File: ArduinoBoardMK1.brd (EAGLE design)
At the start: 95.2 x 82.5 mm, 24 parts

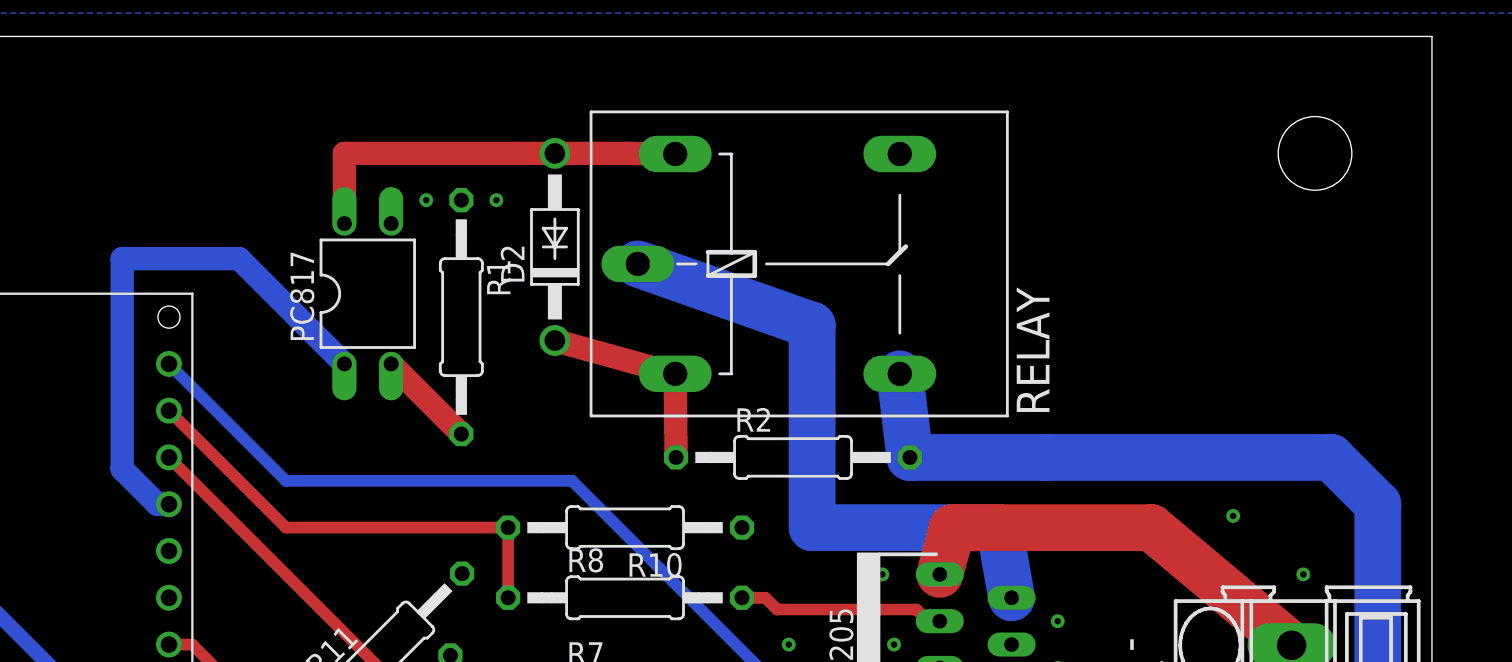
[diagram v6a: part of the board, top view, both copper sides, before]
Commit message: Solid State Relay
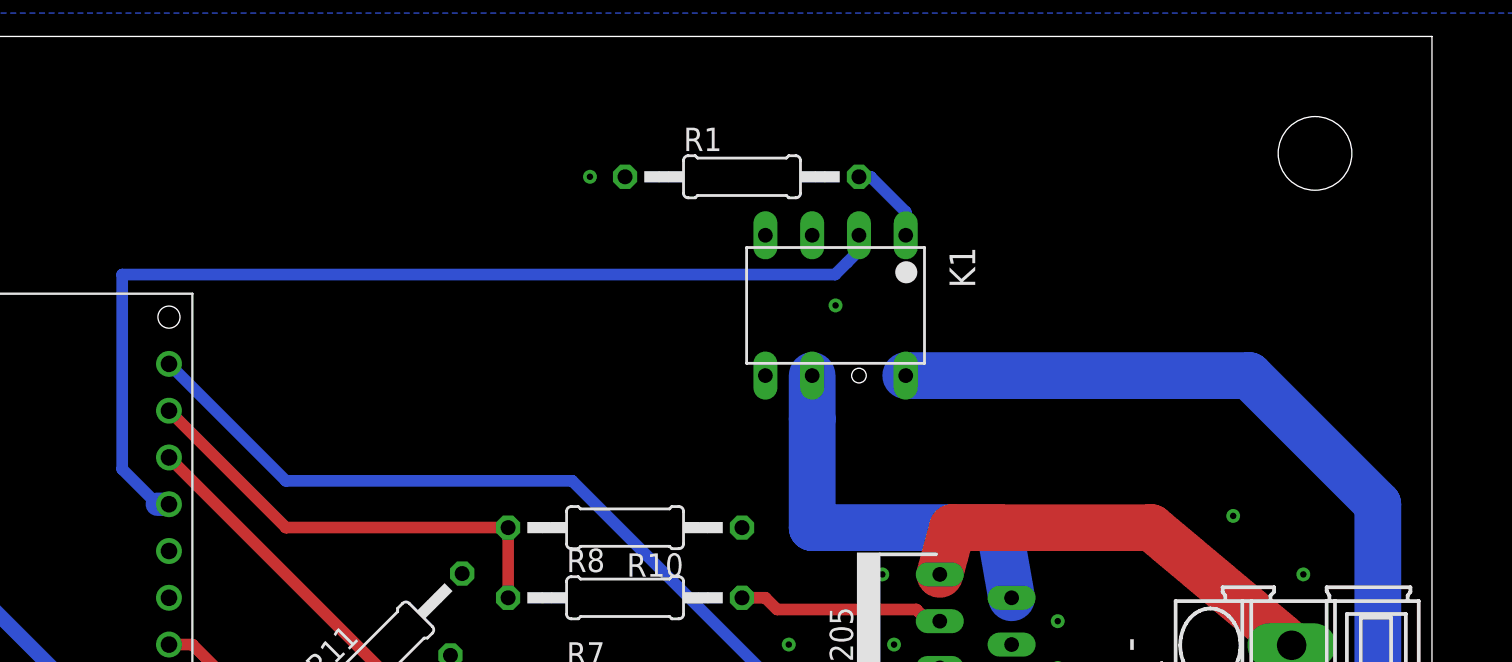
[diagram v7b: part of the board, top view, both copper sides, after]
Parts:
- removed D2: 1N4004, diode:DO41-10
- removed PC817: PC817, optocoupler:DIL04
- removed R2: 220, resistor:0207/12
- removed RELAY: G5LE, relay:G5LE
- added K1: AQH2223, relay:DIL07
- moved R1 17.0 mm to (57.8, 74.9), turned to 0 degrees
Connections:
- removed net FLYBACK-DIODE+: D2.C, R2.1, RELAY.1
- removed net RELAY-TO-OPTO: D2.A, PC817.4, RELAY.2
- net +12V: now also K1.8; no longer R2.2, RELAY.S
- net GND: no longer PC817.3
- net MOTOR-ENABLE: now also K1.2; no longer PC817.1
- net POST-OPTO-DIODE: now also K1.1; no longer PC817.2
- net RELAY-TO-MOTORCONTROLLER: now also K1.6; no longer RELAY.P
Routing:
- net MOTOR-ENABLE: track 29.2 -> 55.3 mm
- net RELAY-TO-OPTO: track 21.8 -> 0.00 mm
- net RELAY-TO-MOTORCONTROLLER: track 35.0 -> 22.3 mm
- net FLYBACK-DIODE+: track 11.3 -> 0.00 mm
- net +12V: track 101.6 -> 99.1 mm
- net POST-OPTO-DIODE: track 5.39 -> 4.60 mm
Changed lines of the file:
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@@
 <drawing>
 <settings>
-<setting alwaysvectorfont="no"/>
+<setting alwaysvectorfont="yes"/>
 <setting verticaltext="up"/>
 </settings>
-<grid distance="0.025" unitdist="inch" unit="mil" style="lines" multiple="1" display="no" altdistance="5" altunitdist="mil" altunit="mil"/>
+<grid distance="0.025" unitdist="inch" unit="inch" style="lines" multiple="1" display="no" altdistance="5" altunitdist="mil" altunit="mil"/>
 <layers>
 <layer number="1" name="Top" color="4" fill="1" visible="yes" active="yes"/>
@@
 <hole x="88.9" y="6.35" drill="4"/>
 <hole x="6.35" y="6.35" drill="4"/>
+<hole x="64.135" y="64.135" drill="0.79501875"/>
 </plain>
 <attributes>
@@
 <element name="R7" library="resistor" library_urn="urn:adsk.eagle:library:348" package="0207/12" package3d_urn="urn:adsk.eagle:package:25938/1" value="1k" x="51.435" y="46.99"/>
 <element name="R8" library="resistor" library_urn="urn:adsk.eagle:library:348" package="0207/12" package3d_urn="urn:adsk.eagle:package:25938/1" value="1k" x="51.435" y="52.07"/>
-<element name="RELAY" library="relay" library_urn="urn:adsk.eagle:library:339" package="G5LE" package3d_urn="urn:adsk.eagle:package:24308/1" value="G5LE" x="61.653509375" y="70.19810625">
-<attribute name="MF" value="" x="61.653509375" y="70.19810625" size="1.778" layer="27" display="off"/>
-<attribute name="MPN" value="" x="61.653509375" y="70.19810625" size="1.778" layer="27" display="off"/>
-<attribute name="OC_FARNELL" value="unknown" x="61.653509375" y="70.19810625" size="1.778" layer="27" display="off"/>
-<attribute name="OC_NEWARK" value="unknown" x="61.653509375" y="70.19810625" size="1.778" layer="27" display="off"/>
-</element>
-<element name="D2" library="diode" library_urn="urn:adsk.eagle:library:210" package="DO41-10" package3d_urn="urn:adsk.eagle:package:43336/1" value="1N4004" x="47.625" y="71.12" rot="R90"/>
 <element name="MOTOR1" library="con-phoenix-smkdsp" library_urn="urn:adsk.eagle:library:180" package="SMKDSP_1,5/2" package3d_urn="urn:adsk.eagle:package:9814/1" value="SMKDSP_1,5/2" x="87.63" y="46.99" rot="R90">
 <attribute name="MF" value="FARNELL" x="87.63" y="46.99" size="1.778" layer="27" rot="R90" display="off"/>
@@
 <attribute name="OC_NEWARK" value="69C8588" x="71.12" y="1.27" size="1.778" layer="27" rot="R90" display="off"/>
 </element>
-<element name="PC817" library="optocoupler" library_urn="urn:adsk.eagle:library:320" package="DIL04" package3d_urn="urn:adsk.eagle:package:21938/1" value="PC817" x="37.465" y="68.58">
-<attribute name="MF" value="" x="37.465" y="68.58" size="1.778" layer="27" display="off"/>
-<attribute name="MPN" value="PC817X4J000F" x="37.465" y="68.58" size="1.778" layer="27" display="off"/>
-<attribute name="OC_FARNELL" value="9707727" x="37.465" y="68.58" size="1.778" layer="27" display="off"/>
-<attribute name="OC_NEWARK" value="97K7059" x="37.465" y="68.58" size="1.778" layer="27" display="off"/>
-</element>
-<element name="R1" library="resistor" library_urn="urn:adsk.eagle:library:348" package="0207/12" package3d_urn="urn:adsk.eagle:package:25938/1" value="220" x="42.545" y="67.31" rot="R270"/>
-<element name="R2" library="resistor" library_urn="urn:adsk.eagle:library:348" package="0207/12" package3d_urn="urn:adsk.eagle:package:25938/1" value="220" x="60.556371875" y="59.69"/>
+<element name="R1" library="resistor" library_urn="urn:adsk.eagle:library:348" package="0207/12" package3d_urn="urn:adsk.eagle:package:25938/1" value="220" x="57.785" y="74.93"/>
 <element name="R3" library="resistor" library_urn="urn:adsk.eagle:library:348" package="0207/12" package3d_urn="urn:adsk.eagle:package:25938/1" value="4.7k" x="11.43" y="14.605" rot="R180"/>
 <element name="TEMPERATURE1" library="SparkFun-Connectors" library_urn="urn:adsk.eagle:library:513" package="1X03_LONGPADS" package3d_urn="urn:adsk.eagle:package:38068/1" value="" x="5.08" y="57.15" rot="R270"/>
@@
 <element name="R6" library="resistor" library_urn="urn:adsk.eagle:library:348" package="0207/12" package3d_urn="urn:adsk.eagle:package:25938/1" value="47k" x="37.465" y="44.45" rot="R225"/>
 <element name="R11" library="resistor" library_urn="urn:adsk.eagle:library:348" package="0207/12" package3d_urn="urn:adsk.eagle:package:25938/1" value="47k" x="38.1" y="48.895" rot="R45"/>
+<element name="K1" library="relay" library_urn="urn:adsk.eagle:library:339" package="DIL07" package3d_urn="urn:adsk.eagle:package:24378/1" value="AQH2223" x="62.865" y="67.945" rot="R180">
+<attribute name="MF" value="AROMAT/ MATSUSHITA" x="62.865" y="67.945" size="1.778" layer="27" rot="R180" display="off"/>
+<attribute name="MPN" value="AQH2223" x="62.865" y="67.945" size="1.778" layer="27" rot="R180" display="off"/>
+<attribute name="OC_FARNELL" value="unknown" x="62.865" y="67.945" size="1.778" layer="27" rot="R180" display="off"/>
+<attribute name="OC_NEWARK" value="26K3059" x="62.865" y="67.945" size="1.778" layer="27" rot="R180" display="off"/>
+</element>
 </elements>
 <signals>
@@
 <contactref element="MICRO" pad="GND"/>
 <contactref element="MICRO" pad="GND1"/>
-<contactref element="PC817" pad="3"/>
 <contactref element="R1" pad="1"/>
 <contactref element="VIN" pad="2"/>
@@
 <via x="84.455" y="56.515" extent="1-16" drill="0.35"/>
 <via x="88.265" y="53.34" extent="1-16" drill="0.35"/>
-<via x="40.64" y="73.66" extent="1-16" drill="0.35"/>
-<via x="44.45" y="73.66" extent="1-16" drill="0.35"/>
+<via x="49.53" y="74.93" extent="1-16" drill="0.35"/>
+<via x="62.865" y="67.945" extent="1-16" drill="0.35"/>
 <via x="5.08" y="16.51" extent="1-16" drill="0.35"/>
 <via x="34.29" y="16.51" extent="1-16" drill="0.35"/>
@@
 </signal>
 <signal name="+12V">
-<contactref element="RELAY" pad="S"/>
 <contactref element="VNH5019" pad="VIN2"/>
 <contactref element="VNH5019" pad="VIN1"/>
 <contactref element="12V" pad="1"/>
-<contactref element="R2" pad="2"/>
-<wire x1="66.352509375" y1="64.22910625" x2="66.906371875" y2="59.69" width="2.54" layer="16"/>
-<wire x1="66.906371875" y1="59.69" x2="74.295" y2="59.69" width="2.54" layer="16"/>
-<wire x1="74.295" y1="59.69" x2="89.769" y2="59.69" width="2.54" layer="16"/>
-<wire x1="92.309" y1="57.15" x2="89.769" y2="59.69" width="2.54" layer="16"/>
+<wire x1="66.675" y1="64.135" x2="85.324" y2="64.135" width="2.54" layer="16"/>
+<wire x1="92.309" y1="57.15" x2="85.324" y2="64.135" width="2.54" layer="16"/>
 <wire x1="87.63" y1="24.17" x2="92.309" y2="24.133159375" width="2.54" layer="16"/>
 <wire x1="92.309" y1="24.133159375" x2="92.309" y2="57.15" width="2.54" layer="16"/>
@@
 <wire x1="74.89" y1="21.59" x2="77.47" y2="24.17" width="2.54" layer="16"/>
 <wire x1="77.47" y1="24.17" x2="87.63" y2="24.17" width="2.54" layer="16"/>
-</signal>
-<signal name="RELAY-TO-OPTO">
-<contactref element="RELAY" pad="2"/>
-<contactref element="D2" pad="A"/>
-<contactref element="PC817" pad="4"/>
-<wire x1="36.195" y1="72.39" x2="36.195" y2="76.2" width="1.27" layer="1"/>
-<wire x1="36.195" y1="76.2" x2="47.625" y2="76.2" width="1.27" layer="1"/>
-<wire x1="54.160509375" y1="76.16710625" x2="51.435" y2="76.2" width="1.27" layer="1"/>
-<wire x1="51.435" y1="76.2" x2="47.625" y2="76.2" width="1.27" layer="1"/>
+<contactref element="K1" pad="8"/>
 </signal>
 <signal name="RELAY-TO-MOTORCONTROLLER">
 <contactref element="TLE5205" pad="6"/>
-<contactref element="RELAY" pad="P"/>
-<wire x1="61.595" y1="66.862503125" x2="52.128509375" y2="70.19810625" width="2.54" layer="16"/>
 <wire x1="71.755" y1="55.88" x2="61.595" y2="55.88" width="2.54" layer="16"/>
-<wire x1="61.595" y1="55.88" x2="61.595" y2="66.862503125" width="2.54" layer="16"/>
+<wire x1="61.595" y1="61.782503125" x2="61.595" y2="55.88" width="2.54" layer="16"/>
 <wire x1="72.425" y1="52.07" x2="71.755" y2="55.88" width="2.54" layer="16"/>
+<contactref element="K1" pad="6"/>
+<wire x1="61.595" y1="64.135" x2="61.595" y2="61.782503125" width="2.54" layer="16"/>
 </signal>
 <signal name="IN1">
@@
 <signal name="MOTOR-ENABLE">
 <contactref element="MICRO" pad="D9"/>
-<contactref element="PC817" pad="1"/>
-<wire x1="24.13" y1="70.485" x2="24.13" y2="59.055" width="1.27" layer="16"/>
-<wire x1="30.48" y1="70.485" x2="24.13" y2="70.485" width="1.27" layer="16"/>
-<wire x1="36.195" y1="64.77" x2="30.48" y2="70.485" width="1.27" layer="16"/>
-<wire x1="24.13" y1="59.055" x2="26.035" y2="57.15" width="1.27" layer="16"/>
+<wire x1="24.13" y1="69.6215" x2="24.13" y2="59.055" width="0.635" layer="16"/>
+<wire x1="24.13" y1="69.6215" x2="62.84283125" y2="69.6215" width="0.635" layer="16"/>
+<wire x1="24.13" y1="59.055" x2="26.035" y2="57.15" width="0.635" layer="16"/>
 <wire x1="26.035" y1="57.15" x2="26.67" y2="57.15" width="1.27" layer="16"/>
+<contactref element="K1" pad="2"/>
+<wire x1="63.495165625" y1="70.273834375" x2="64.135" y2="70.91366875" width="0.635" layer="16"/>
+<wire x1="64.135" y1="70.91366875" x2="64.135" y2="71.755" width="0.635" layer="16"/>
+<wire x1="62.84283125" y1="69.6215" x2="63.495165625" y2="70.273834375" width="0.635" layer="16"/>
 </signal>
 <signal name="PELTIER-OUTB">
@@
 <signal name="POST-OPTO-DIODE">
 <contactref element="R1" pad="2"/>
-<contactref element="PC817" pad="2"/>
-<wire x1="38.735" y1="64.77" x2="42.545" y2="60.96" width="1.27" layer="1"/>
-</signal>
-<signal name="FLYBACK-DIODE+">
-<contactref element="RELAY" pad="1"/>
-<contactref element="D2" pad="C"/>
-<contactref element="R2" pad="1"/>
-<wire x1="47.625" y1="66.04" x2="54.160509375" y2="64.22910625" width="1.27" layer="1"/>
-<wire x1="54.206371875" y1="59.69" x2="54.160509375" y2="64.22910625" width="1.27" layer="1"/>
+<contactref element="K1" pad="1"/>
+<wire x1="66.675" y1="71.755" x2="66.675" y2="73.025" width="0.635" layer="16"/>
+<wire x1="66.675" y1="73.025" x2="64.77" y2="74.93" width="0.635" layer="16"/>
+<wire x1="64.77" y1="74.93" x2="64.135" y2="74.93" width="0.635" layer="16"/>
 </signal>
 <signal name="TEMPERATURE2">

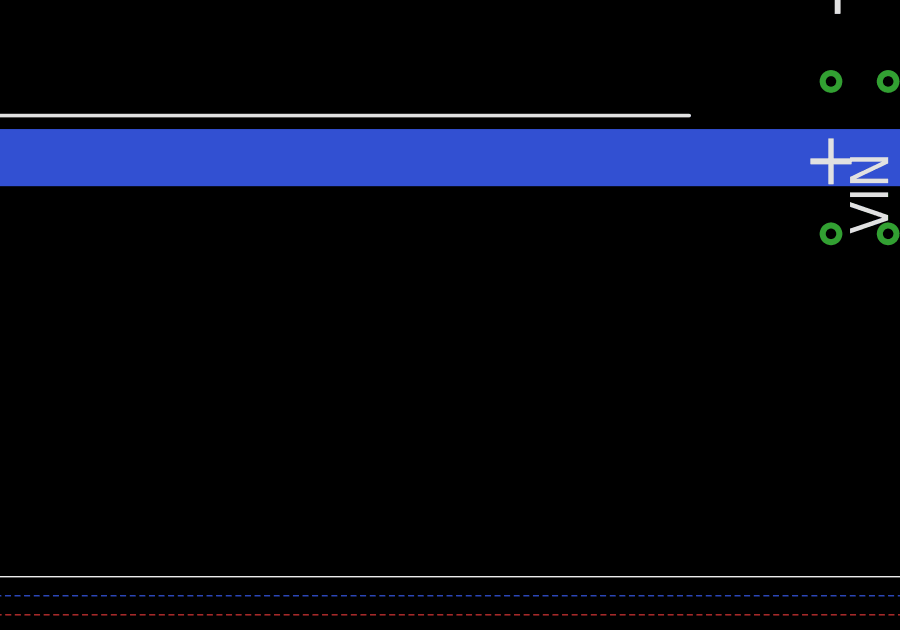
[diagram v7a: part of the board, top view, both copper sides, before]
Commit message: Display Board. Attained old board files. Schematic organization.
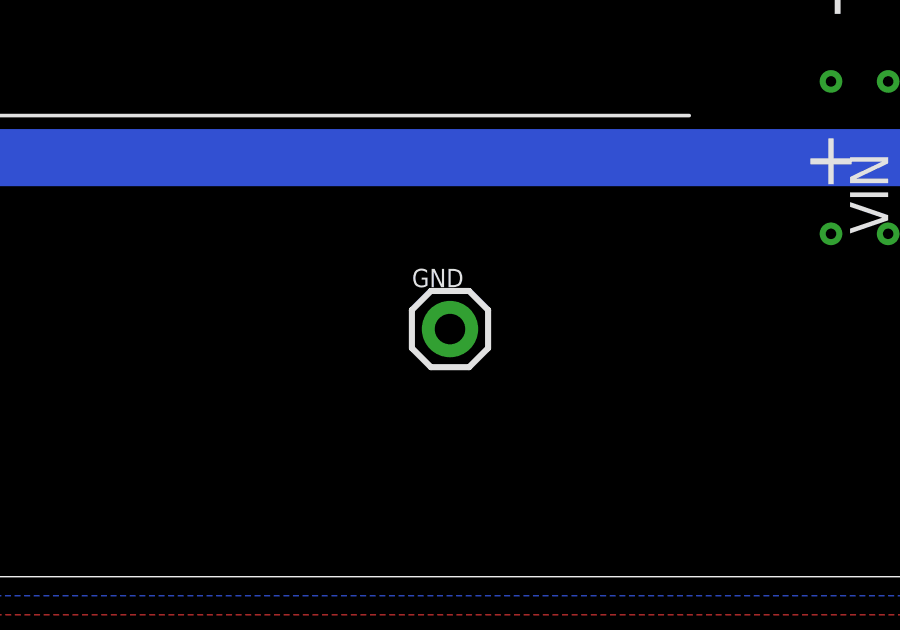
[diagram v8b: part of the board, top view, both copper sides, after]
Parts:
- added GND: (no value), SparkFun-Connectors:1X01
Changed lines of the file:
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@@
 <drawing>
 <settings>
-<setting alwaysvectorfont="yes"/>
+<setting alwaysvectorfont="no"/>
 <setting verticaltext="up"/>
 </settings>
@@
 <attribute name="OC_NEWARK" value="26K3059" x="62.865" y="67.945" size="1.778" layer="27" rot="R180" display="off"/>
 </element>
+<element name="GND" library="SparkFun-Connectors" library_urn="urn:adsk.eagle:library:513" package="1X01" package3d_urn="urn:adsk.eagle:package:38028/1" value="" x="66.04" y="8.255"/>
 </elements>
 <signals>
